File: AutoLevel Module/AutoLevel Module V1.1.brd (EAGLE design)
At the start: 22.5 x 12.5 mm, 10 parts

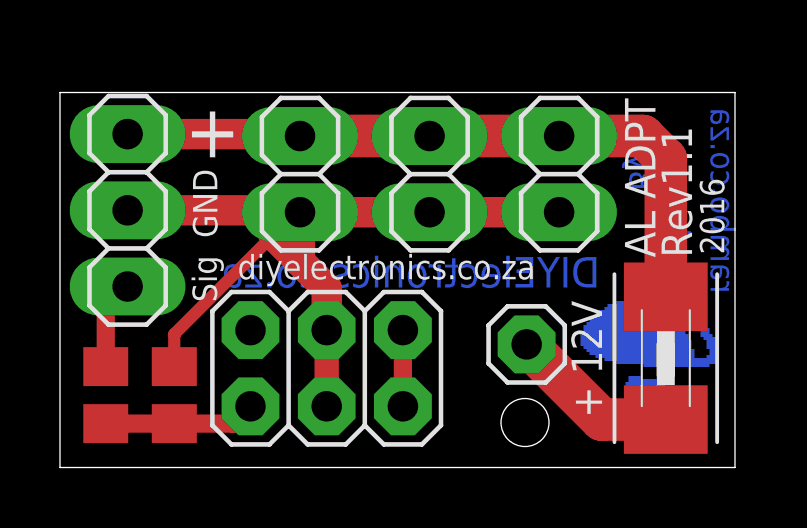
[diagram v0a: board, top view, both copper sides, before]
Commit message: Ordered new AL boards
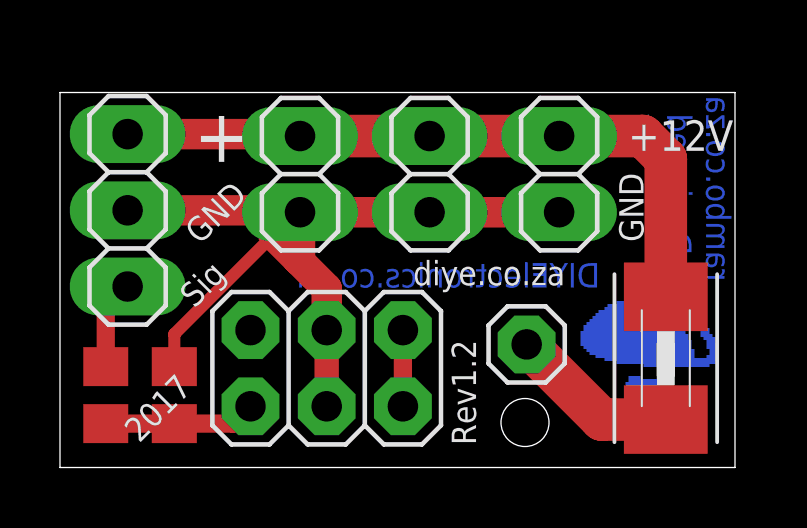
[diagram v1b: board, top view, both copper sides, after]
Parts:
- added U$2: SHROOMBOTTOMSILK, RobThePyro:SHROOM_BS
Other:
- board text added: "+12V"
- board text added: "2017"
- board text added: "Rev1.2"
- board text added: "diye.co.za"
- board text removed: "+ 12V"
- board text removed: "2016"
- board text removed: "Rev1.1"
- board text removed: "diyelectronics.co.za"
